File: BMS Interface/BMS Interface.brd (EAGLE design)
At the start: 57.1 x 82.5 mm, 23 parts

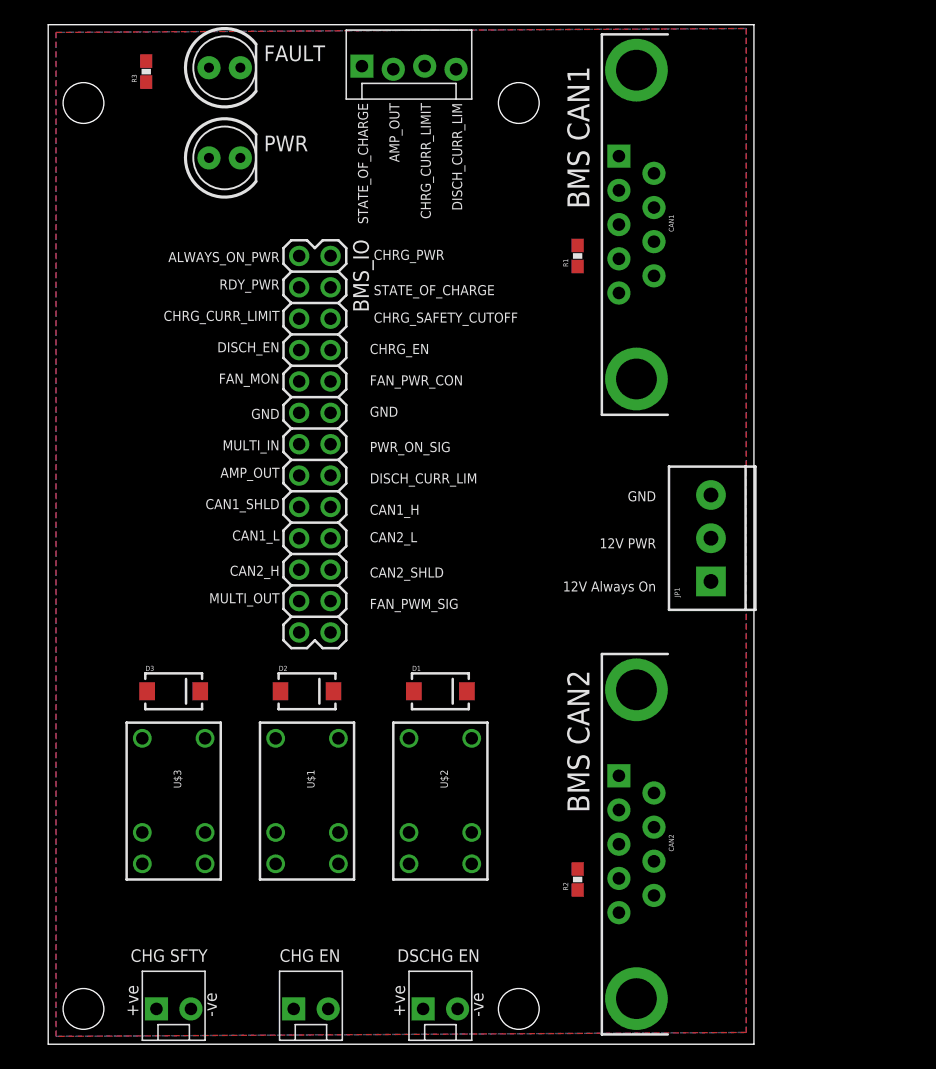
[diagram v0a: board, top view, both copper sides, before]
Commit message: Moved BMS interface to use an ATX connector.
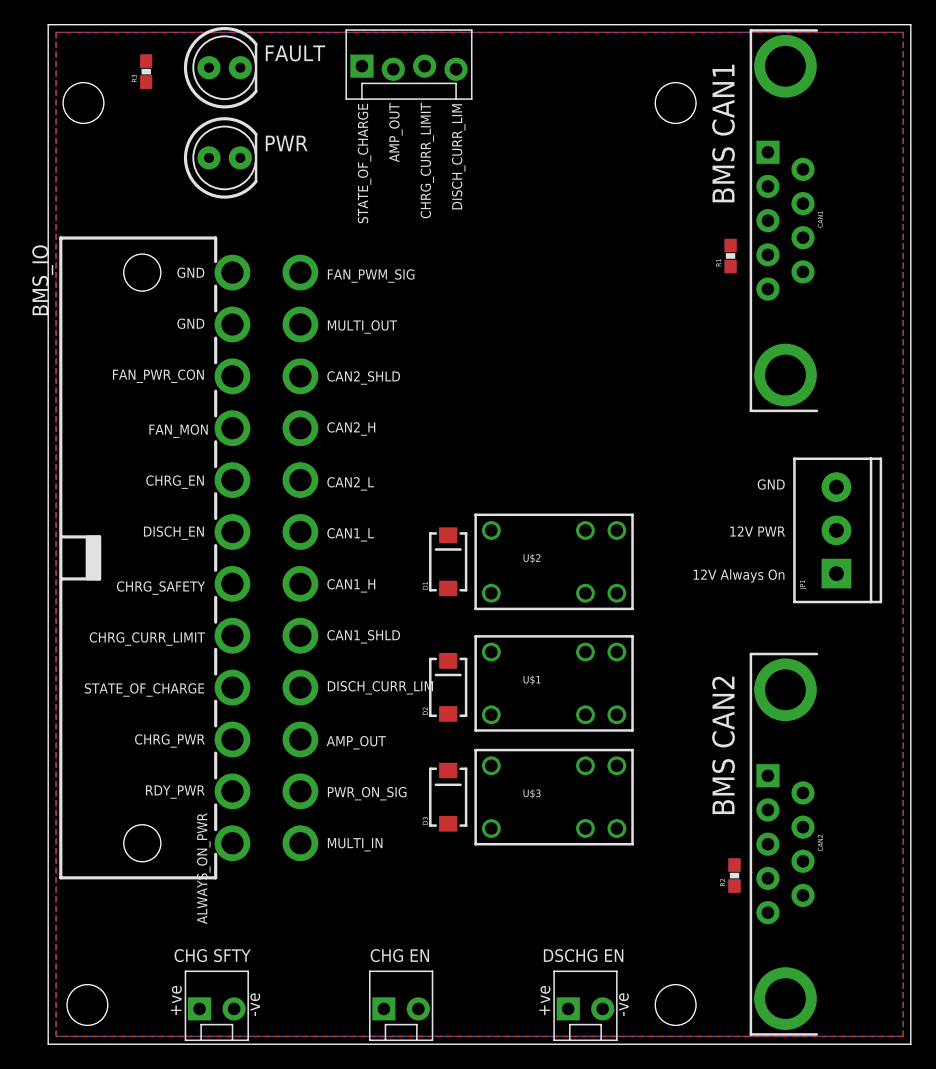
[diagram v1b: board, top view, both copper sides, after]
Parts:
- BMS_IO: value M13X22X13 -> ATX24RH; device SparkFun-Connectors:2X13 -> SparkFun-Connectors:ATX24_RIGHT_ANGLE
- moved U$3 30.8 mm to (41.0, 20.0), turned to 0 degrees
- moved BMS_IO 26.5 mm to (10.2, 39.4)
- moved D3 23.8 mm to (32.4, 20.0), turned to 90 degrees
- moved U$1 22.2 mm to (41.0, 29.2), turned to 0 degrees
- moved U$2 21.4 mm to (41.0, 39.1), turned to 0 degrees
- moved R2 12.7 mm to (55.6, 13.7)
- moved STANDOFF3 12.7 mm to (50.8, 3.17)
- moved STANDOFF4 12.7 mm to (50.8, 76.2)
- moved R1 12.4 mm to (55.2, 63.8)
- moved CAN1 12.1 mm to (59.7, 66.7)
- moved CAN2 12.1 mm to (59.7, 16.2)
- moved PACK_CONTACTOR 11.7 mm to (42.2, 2.86)
- moved D2 11.4 mm to (32.4, 28.9), turned to 90 degrees
- moved D1 10.5 mm to (32.4, 39.1), turned to 90 degrees
- moved JP1 10.2 mm to (63.8, 38.1)
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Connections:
- removed net N$13: BMS_IO.25
- removed net N$26: BMS_IO.26
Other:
- board size 57.1 x 82.5 mm -> 69.8 x 82.5 mm
- board text added: "CHRG_SAFETY"
- board text removed: "CHRG_SAFETY_CUTOFF"

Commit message: Routed BMS interface board and added branding.
Changed branding for CCB and MCBs
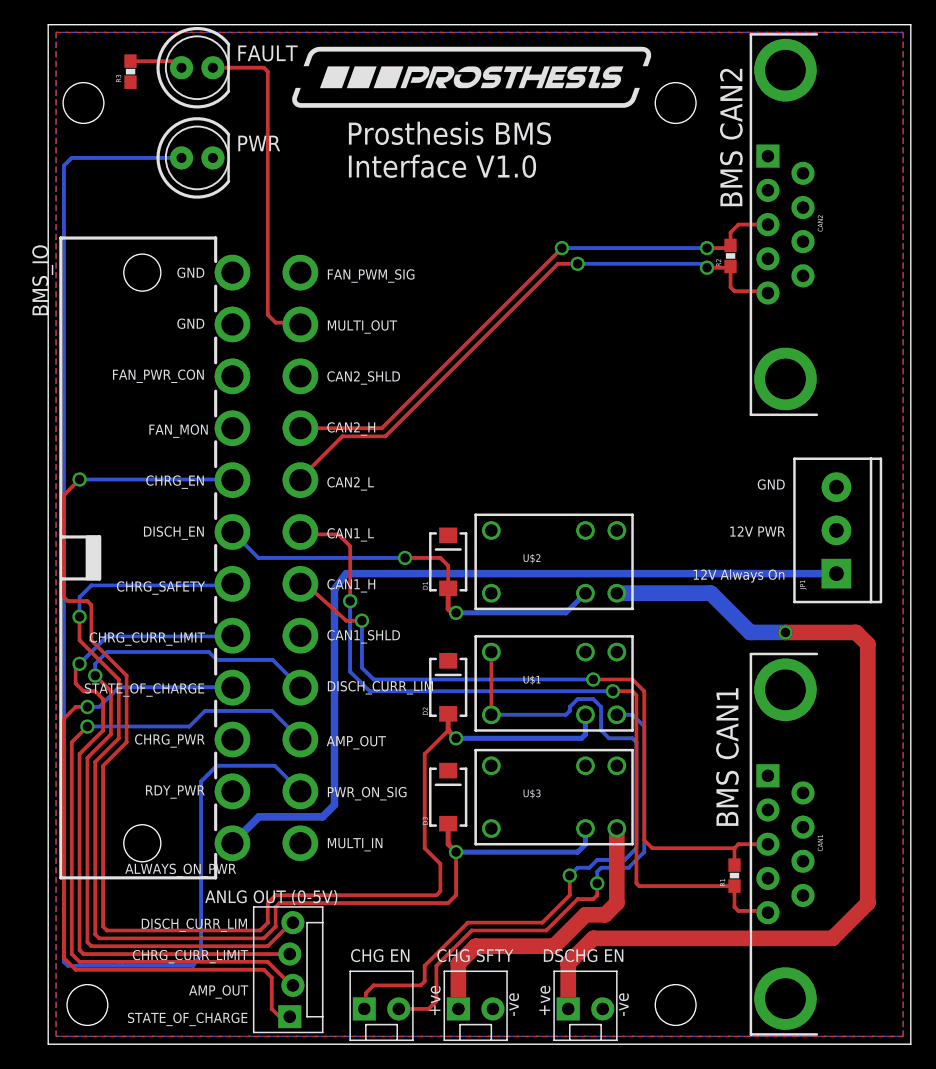
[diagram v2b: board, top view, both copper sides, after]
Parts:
- added U$4: (no value), prosthesis:PROS_LOGO
- moved ANALOG_OUT 77.0 mm to (19.7, 2.22), turned to 90 degrees
- moved CAN1 50.5 mm to (59.7, 16.2)
- moved R1 50.2 mm to (55.6, 13.7)
- moved R2 50.2 mm to (55.2, 63.8)
- moved CAN2 50.2 mm to (59.7, 66.4)
- moved PACK_CHARGE_SFTY 21.0 mm to (33.3, 2.86)
- moved FAULT 2.22 mm to (12.1, 79.1)
- moved PWR 2.22 mm to (12.1, 71.8)
- moved PACK_CHARGE_EN 1.59 mm to (25.7, 2.86)
- moved R3 1.27 mm to (6.67, 78.7)
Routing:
- net CHARGE_ENABLE: track 0.00 -> 111.4 mm, vias 0 -> 2
- net POWER_ON_SIGNAL: track 0.00 -> 109.4 mm
- net CHARGE_SAFETY: track 0.00 -> 92.0 mm, vias 0 -> 2
- net PACK_CONTACT_OUT: track 0.00 -> 72.9 mm, vias 0 -> 1
- net ALWAYS_ON_PWR: track 0.00 -> 68.3 mm
- net CAN1_L: track 0.00 -> 66.5 mm, vias 0 -> 2
- net DISCHARGE_CURRENT_LIMIT: track 0.00 -> 59.6 mm, vias 0 -> 1
- net PACK_CHARGE_IN: track 0.00 -> 58.4 mm, vias 0 -> 1
- net CAN1_H: track 0.00 -> 57.4 mm, vias 0 -> 2
- net AMPERAGE_OUT: track 0.00 -> 56.6 mm, vias 0 -> 1
- net CHARGE_CURRENT_LIMIT: track 0.00 -> 56.0 mm, vias 0 -> 1
- net STATE_OF_CHARGE: track 0.00 -> 55.8 mm, vias 0 -> 1
- net CAN2_L: track 0.00 -> 47.2 mm, vias 0 -> 2
- net CAN2_H: track 0.00 -> 45.3 mm, vias 0 -> 2
- net PACK_CHARGE_OUT: track 0.00 -> 40.7 mm, vias 0 -> 1
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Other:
- board text added: "ANLG OUT (0-5V)"
- board text added: "Prosthesis BMS Interface V1.0"
